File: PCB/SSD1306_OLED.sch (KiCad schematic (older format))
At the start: 1 part, among them J5 OLED_I2C

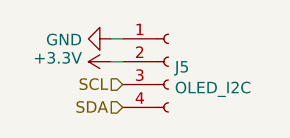
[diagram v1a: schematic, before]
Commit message: Increased VCC from 3v3 to 5v
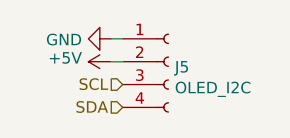
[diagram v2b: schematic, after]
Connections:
- net +3V3 renamed +5V
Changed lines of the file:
@@
 Wire Wire Line
 	5600 3950 5650 3950
-$Comp
-L power:+3.3V #PWR055
-U 1 1 5E86671F
-P 5600 4050
-F 0 "#PWR055" H 5600 3900 50  0001 C CNN
-F 1 "+3.3V" V 5615 4178 50  0000 L CNN
-F 2 "" H 5600 4050 50  0001 C CNN
-F 3 "" H 5600 4050 50  0001 C CNN
-	1    5600 4050
-	0    -1   -1   0
-$EndComp
 Wire Wire Line
 	5600 4050 5650 4050
@@
 Text HLabel 5650 4250 0    50   Input ~ 0
 SDA
+$Comp
+L power:+5V #PWR?
+U 1 1 5E91D05A
+P 5600 4050
+AR Path="/5E8A6686/5E91D05A" Ref="#PWR?"  Part="1"
+AR Path="/5E8F3A13/5E91D05A" Ref="#PWR?"  Part="1"
+F 0 "#PWR?" H 5600 3900 50  0001 C CNN
+F 1 "+5V" V 5615 4178 50  0000 L CNN
+F 2 "" H 5600 4050 50  0001 C CNN
+F 3 "" H 5600 4050 50  0001 C CNN
+	1    5600 4050
+	0    -1   -1   0
+$EndComp
 $EndSCHEMATC

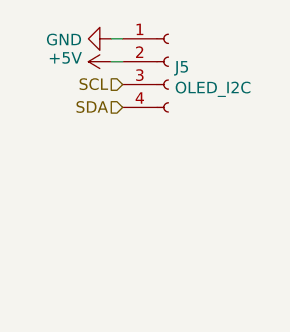
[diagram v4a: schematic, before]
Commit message: Added SPI OLED display
the I2C bus is pretty bloated and will be slow to update
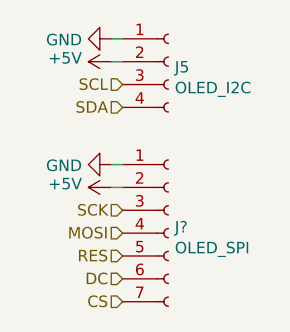
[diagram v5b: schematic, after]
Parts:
- added J?: OLED_SPI, symbol Connector:Conn_01x07_Female
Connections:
- net +5V: now also J?.2 (Pin_2)
- net GND: now also J?.1 (Pin_1)
- new net CS: J?.7 (Pin_7)
- new net DC: J?.6 (Pin_6)
- new net MOSI: J?.4 (Pin_4)
- new net RES: J?.5 (Pin_5)
- new net SCK: J?.3 (Pin_3)
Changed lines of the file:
@@
 $Descr A4 11693 8268
 encoding utf-8
-Sheet 6 26
+Sheet 6 22
 Title ""
 Date ""
@@
 	0    -1   -1   0
 $EndComp
+$Comp
+L Connector:Conn_01x07_Female J?
+U 1 1 5E95B0C8
+P 5850 4800
+F 0 "J?" H 5878 4826 50  0000 L CNN
+F 1 "OLED_SPI" H 5878 4735 50  0000 L CNN
+F 2 "" H 5850 4800 50  0001 C CNN
+F 3 "~" H 5850 4800 50  0001 C CNN
+	1    5850 4800
+	1    0    0    -1
+$EndComp
+$Comp
+L power:GND #PWR?
+U 1 1 5E95B74C
+P 5600 4500
+F 0 "#PWR?" H 5600 4250 50  0001 C CNN
+F 1 "GND" V 5605 4372 50  0000 R CNN
+F 2 "" H 5600 4500 50  0001 C CNN
+F 3 "" H 5600 4500 50  0001 C CNN
+	1    5600 4500
+	0    1    1    0
+$EndComp
+$Comp
+L power:+5V #PWR?
+U 1 1 5E95B8FC
+P 5600 4600
+AR Path="/5E8A6686/5E95B8FC" Ref="#PWR?"  Part="1"
+AR Path="/5E8F3A13/5E95B8FC" Ref="#PWR?"  Part="1"
+F 0 "#PWR?" H 5600 4450 50  0001 C CNN
+F 1 "+5V" V 5615 4728 50  0000 L CNN
+F 2 "" H 5600 4600 50  0001 C CNN
+F 3 "" H 5600 4600 50  0001 C CNN
+	1    5600 4600
+	0    -1   -1   0
+$EndComp
+Wire Wire Line
+	5600 4600 5650 4600
+Wire Wire Line
+	5600 4500 5650 4500
+Text HLabel 5650 4800 0    50   Input ~ 0
+MOSI
+Text HLabel 5650 4700 0    50   Input ~ 0
+SCK
+Text HLabel 5650 5000 0    50   Input ~ 0
+DC
+Text HLabel 5650 5100 0    50   Input ~ 0
+CS
+Text HLabel 5650 4900 0    50   Input ~ 0
+RES
 $EndSCHEMATC

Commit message: Added IEC connector and organised
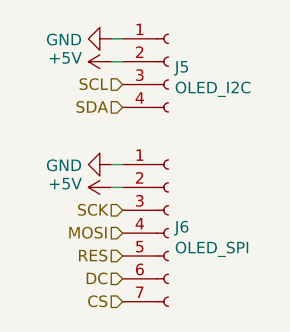
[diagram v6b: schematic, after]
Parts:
- gave numbers to parts that had none: 1
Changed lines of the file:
@@
 $EndComp
 $Comp
-L Connector:Conn_01x07_Female J?
+L Connector:Conn_01x07_Female J6
 U 1 1 5E95B0C8
 P 5850 4800
-F 0 "J?" H 5878 4826 50  0000 L CNN
+F 0 "J6" H 5878 4826 50  0000 L CNN
 F 1 "OLED_SPI" H 5878 4735 50  0000 L CNN
 F 2 "" H 5850 4800 50  0001 C CNN
@@
 $EndComp
 $Comp
-L power:GND #PWR?
+L power:GND #PWR063
 U 1 1 5E95B74C
 P 5600 4500
-F 0 "#PWR?" H 5600 4250 50  0001 C CNN
+F 0 "#PWR063" H 5600 4250 50  0001 C CNN
 F 1 "GND" V 5605 4372 50  0000 R CNN
 F 2 "" H 5600 4500 50  0001 C CNN
@@
 P 5600 4600
 AR Path="/5E8A6686/5E95B8FC" Ref="#PWR?"  Part="1"
-AR Path="/5E8F3A13/5E95B8FC" Ref="#PWR?"  Part="1"
-F 0 "#PWR?" H 5600 4450 50  0001 C CNN
+AR Path="/5E8F3A13/5E95B8FC" Ref="#PWR064"  Part="1"
+F 0 "#PWR064" H 5600 4450 50  0001 C CNN
 F 1 "+5V" V 5615 4728 50  0000 L CNN
 F 2 "" H 5600 4600 50  0001 C CNN

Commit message: Swapped MSx jumpers around so that fullstep is default
The footprint used defaults to bridging pins 2 and 3
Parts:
- J5: footprint (none) -> Connector_PinHeader_2.54mm:PinHeader_1x04_P2.54mm_Vertical
- J6: footprint (none) -> Connector_PinHeader_2.54mm:PinHeader_1x07_P2.54mm_Vertical
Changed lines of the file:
@@
 F 0 "J5" H 5878 4026 50  0000 L CNN
 F 1 "OLED_I2C" H 5878 3935 50  0000 L CNN
-F 2 "" H 5850 4050 50  0001 C CNN
+F 2 "Connector_PinHeader_2.54mm:PinHeader_1x04_P2.54mm_Vertical" H 5850 4050 50  0001 C CNN
 F 3 "" H 5850 4050 50  0001 C CNN
 	1    5850 4050
@@
 F 0 "J6" H 5878 4826 50  0000 L CNN
 F 1 "OLED_SPI" H 5878 4735 50  0000 L CNN
-F 2 "" H 5850 4800 50  0001 C CNN
+F 2 "Connector_PinHeader_2.54mm:PinHeader_1x07_P2.54mm_Vertical" H 5850 4800 50  0001 C CNN
 F 3 "~" H 5850 4800 50  0001 C CNN
 	1    5850 4800
